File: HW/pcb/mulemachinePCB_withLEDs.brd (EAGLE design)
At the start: 68.6 x 54.6 mm, 33 parts, among them IC1 LD117AV50, IC2 MEGA8-P, J1 DCJ0202, Q1 16Mhz

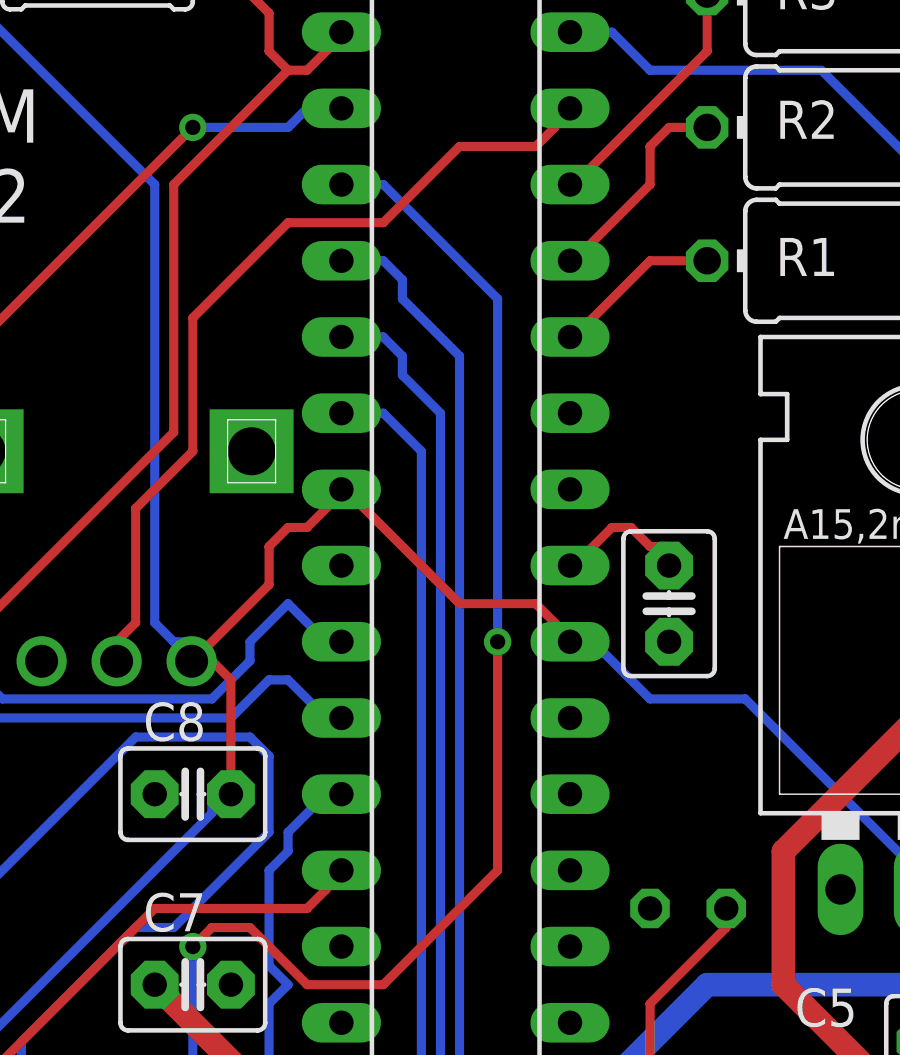
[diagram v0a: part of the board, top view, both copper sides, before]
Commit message: repinned LED and pump pins on MCU to use PWM digital pins. need to check and then reroute PCB and redo GND planes
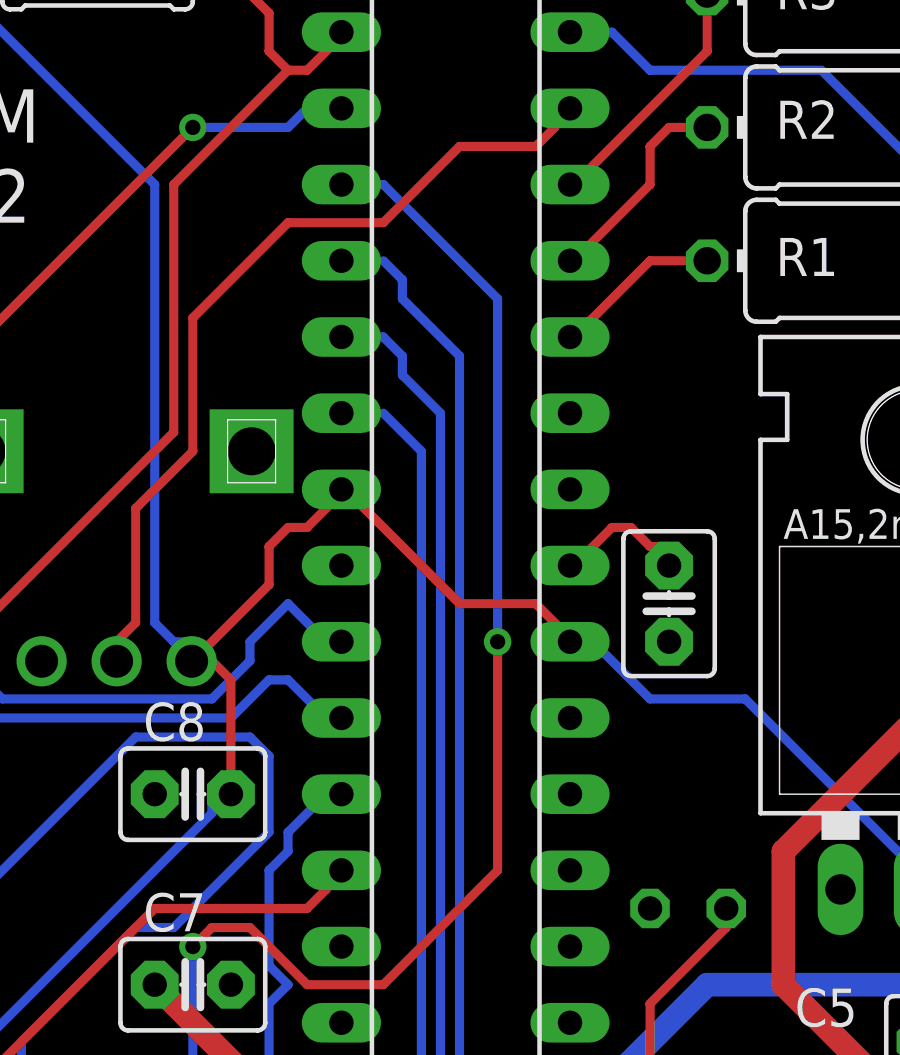
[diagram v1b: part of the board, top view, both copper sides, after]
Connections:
- net LED_YELLOW renamed LED_YELLOW_PWM
- removed net LED_GREEN: IC2.4, R6.1
- removed net PUMP_GB: IC2.25, R2.1
- removed net PUMP_LIME: IC2.26, R3.1
- removed net PUMP_VODKA: IC2.24, R1.1
- new net LED_GREEN_PWM: IC2.11, R6.1
- new net LED_ORANGE_PWM: IC2.12
- new net PUMP_GB_PWM: IC2.16, R2.1
- new net PUMP_LIME_PWM: IC2.17, R3.1
- new net PUMP_VODKA_PWM: IC2.15, R1.1
- net CUPSENSOR: now also IC2.6; no longer IC2.11
- net LED_ORANGE: no longer IC2.6
- net MANUALOVERRIDE: now also IC2.13; no longer IC2.12
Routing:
- net LED_GREEN: track 52.4 -> 0.00 mm, vias 1 -> 0
- net LED_GREEN_PWM: track 0.00 -> 51.0 mm, vias 0 -> 1
- net PUMP_LIME: track 8.32 -> 0.00 mm
- net PUMP_LIME_PWM: track 0.00 -> 8.19 mm
- net PUMP_GB: track 7.16 -> 0.00 mm
- net PUMP_GB_PWM: track 0.00 -> 7.03 mm
- net PUMP_VODKA: track 5.62 -> 0.00 mm
- net PUMP_VODKA_PWM: track 0.00 -> 5.50 mm
- net LED_ORANGE: track 27.7 -> 26.3 mm
- net CUPSENSOR: track 50.6 -> 50.1 mm
- net MANUALOVERRIDE: track 30.7 -> 30.1 mm
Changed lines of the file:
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@@
 <contactref element="T1" pad="E"/>
 <contactref element="T2" pad="E"/>
-<contactref element="T3" pad="E"/>
 <contactref element="C5" pad="2"/>
 <contactref element="C6" pad="-"/>
@@
 <contactref element="C3" pad="2"/>
 <contactref element="C2" pad="2"/>
-<wire x1="5.3594" y1="10.8712" x2="5.3594" y2="4.3688" width="0" layer="19" extent="1-1"/>
+<contactref element="T3" pad="E"/>
+<wire x1="55.88" y1="51.435" x2="60.96" y2="51.435" width="0" layer="19" extent="1-1"/>
+<wire x1="50.8" y1="51.435" x2="55.88" y2="51.435" width="0" layer="19" extent="1-1"/>
+<wire x1="62.865" y1="41.91" x2="60.96" y2="51.435" width="0" layer="19" extent="1-1"/>
+<wire x1="62.865" y1="33.02" x2="62.865" y2="41.91" width="0" layer="19" extent="1-1"/>
+<wire x1="58.42" y1="21.59" x2="62.865" y2="33.02" width="0" layer="19" extent="1-1"/>
+<wire x1="50.84" y1="29.83" x2="58.42" y2="21.59" width="0" layer="19" extent="1-1"/>
+<wire x1="56.4388" y1="10.414" x2="58.42" y2="21.59" width="0" layer="19" extent="1-1"/>
+<wire x1="44.577" y1="17.145" x2="56.4388" y2="10.414" width="0" layer="19" extent="1-1"/>
+<wire x1="39.37" y1="22.225" x2="44.577" y2="17.145" width="0" layer="19" extent="1-1"/>
+<wire x1="33.02" y1="21.59" x2="39.37" y2="22.225" width="0" layer="19" extent="1-1"/>
+<wire x1="33.655" y1="30.48" x2="33.02" y2="21.59" width="0" layer="19" extent="1-1"/>
+<wire x1="30.353" y1="35.56" x2="33.655" y2="30.48" width="0" layer="19" extent="1-1"/>
+<wire x1="22.733" y1="33.02" x2="30.353" y2="35.56" width="0" layer="19" extent="1-1"/>
+<wire x1="16.51" y1="25.4" x2="22.733" y2="33.02" width="0" layer="19" extent="1-1"/>
+<wire x1="12.74" y1="29.83" x2="16.51" y2="25.4" width="0" layer="19" extent="1-1"/>
+<wire x1="19.05" y1="19.05" x2="16.51" y2="25.4" width="0" layer="19" extent="1-1"/>
+<wire x1="4.953" y1="27.94" x2="12.74" y2="29.83" width="0" layer="19" extent="1-1"/>
+<wire x1="7.62" y1="21.59" x2="4.953" y2="27.94" width="0" layer="19" extent="1-1"/>
+<wire x1="5.3594" y1="10.8712" x2="7.62" y2="21.59" width="0" layer="19" extent="1-1"/>
+<wire x1="5.3594" y1="4.3688" x2="5.3594" y2="10.8712" width="0" layer="19" extent="1-1"/>
+<wire x1="2.54" y1="3.048" x2="5.3594" y2="4.3688" width="0" layer="19" extent="1-1"/>
+<wire x1="35.026" y1="10.668" x2="33.02" y2="21.59" width="0" layer="19" extent="1-1"/>
+<wire x1="30.226" y1="7.668" x2="35.026" y2="10.668" width="0" layer="19" extent="1-1"/>
+<wire x1="4.953" y1="44.45" x2="4.953" y2="27.94" width="0" layer="19" extent="1-1"/>
 </signal>
 <signal name="VCC" class="1">
@@
 <signal name="CUPSENSOR">
 <contactref element="X2" pad="7"/>
-<contactref element="IC2" pad="11"/>
 <wire x1="20.955" y1="24.13" x2="22.225" y2="25.4" width="0.3048" layer="16"/>
 <wire x1="20.955" y1="23.495" x2="20.955" y2="24.13" width="0.3048" layer="16"/>
@@
 <wire x1="51.435" y1="7.62" x2="34.29" y2="7.62" width="0.3048" layer="16"/>
 <wire x1="53.975" y1="10.16" x2="51.435" y2="7.62" width="0.3048" layer="16"/>
-<wire x1="22.225" y1="25.4" x2="22.733" y2="25.4" width="0.3048" layer="16"/>
 <wire x1="53.975" y1="10.16" x2="53.6956" y2="10.414" width="0.3048" layer="16"/>
+<contactref element="IC2" pad="6"/>
+<wire x1="22.225" y1="25.4" x2="22.733" y2="38.1" width="0" layer="19" extent="16-16"/>
 </signal>
 <signal name="N$12">
@@
 </signal>
 <signal name="MANUALOVERRIDE">
-<contactref element="IC2" pad="12"/>
 <contactref element="S2" pad="3"/>
 <contactref element="S2" pad="4"/>
@@
 <wire x1="8.89" y1="12.7" x2="8.89" y2="13.97" width="0.3048" layer="1"/>
 <wire x1="10.16" y1="11.43" x2="8.89" y2="12.7" width="0.3048" layer="1"/>
-<wire x1="22.225" y1="22.86" x2="22.733" y2="22.86" width="0.3048" layer="1"/>
 <wire x1="10.16" y1="11.43" x2="9.8806" y2="10.8712" width="0.3048" layer="1"/>
 <wire x1="9.525" y1="5.715" x2="9.525" y2="4.445" width="0.3048" layer="1"/>
@@
 <wire x1="9.525" y1="4.445" x2="9.8806" y2="4.3688" width="0.3048" layer="1"/>
 <wire x1="9.525" y1="11.43" x2="9.8806" y2="10.8712" width="0.3048" layer="1"/>
-</signal>
-<signal name="PUMP_VODKA">
-<contactref element="IC2" pad="24"/>
+<contactref element="IC2" pad="13"/>
+<wire x1="22.225" y1="22.86" x2="22.733" y2="20.32" width="0" layer="19" extent="1-1"/>
+</signal>
+<signal name="PUMP_VODKA_PWM">
 <contactref element="R1" pad="1"/>
 <wire x1="33.02" y1="43.18" x2="30.48" y2="40.64" width="0.3048" layer="1"/>
 <wire x1="34.925" y1="43.18" x2="33.02" y2="43.18" width="0.3048" layer="1"/>
-<wire x1="30.48" y1="40.64" x2="30.353" y2="40.64" width="0.3048" layer="1"/>
-</signal>
-<signal name="PUMP_GB">
-<contactref element="IC2" pad="25"/>
+<contactref element="IC2" pad="15"/>
+<wire x1="30.353" y1="17.78" x2="30.48" y2="40.64" width="0" layer="19" extent="1-1"/>
+</signal>
+<signal name="PUMP_GB_PWM">
 <contactref element="R2" pad="1"/>
 <wire x1="33.02" y1="45.72" x2="30.48" y2="43.18" width="0.3048" layer="1"/>
@@
 <wire x1="33.655" y1="47.625" x2="33.02" y2="46.99" width="0.3048" layer="1"/>
 <wire x1="34.925" y1="47.625" x2="33.655" y2="47.625" width="0.3048" layer="1"/>
-<wire x1="30.48" y1="43.18" x2="30.353" y2="43.18" width="0.3048" layer="1"/>
-</signal>
-<signal name="PUMP_LIME">
-<contactref element="IC2" pad="26"/>
+<contactref element="IC2" pad="16"/>
+<wire x1="30.353" y1="20.32" x2="30.48" y2="43.18" width="0" layer="19" extent="1-1"/>
+</signal>
+<signal name="PUMP_LIME_PWM">
 <contactref element="R3" pad="1"/>
 <wire x1="34.925" y1="50.165" x2="30.48" y2="45.72" width="0.3048" layer="1"/>
 <wire x1="34.925" y1="52.07" x2="34.925" y2="50.165" width="0.3048" layer="1"/>
-<wire x1="30.48" y1="45.72" x2="30.353" y2="45.72" width="0.3048" layer="1"/>
+<contactref element="IC2" pad="17"/>
+<wire x1="30.353" y1="22.86" x2="30.48" y2="45.72" width="0" layer="19" extent="1-1"/>
 </signal>
 <signal name="PUMP_LIME_VCC" class="1">
@@
 <wire x1="57.15" y1="15.24" x2="55.245" y2="17.145" width="0.7874" layer="1"/>
 </signal>
-<signal name="LED_GREEN">
+<signal name="LED_GREEN_PWM">
 <contactref element="R6" pad="1"/>
-<contactref element="IC2" pad="4"/>
-<wire x1="24.13" y1="43.18" x2="22.733" y2="43.18" width="0.3048" layer="16"/>
 <wire x1="24.765" y1="42.545" x2="24.13" y2="43.18" width="0.3048" layer="16"/>
 <wire x1="24.765" y1="41.91" x2="24.765" y2="42.545" width="0.3048" layer="16"/>
@@
 <wire x1="12.065" y1="3.175" x2="17.78" y2="3.175" width="0.3048" layer="1"/>
 <via x="27.305" y="14.605" extent="1-16" drill="0.508"/>
-</signal>
-<signal name="LED_YELLOW">
+<contactref element="IC2" pad="11"/>
+<wire x1="27.305" y1="14.605" x2="22.733" y2="25.4" width="0" layer="19" extent="1-1"/>
+</signal>
+<signal name="LED_YELLOW_PWM">
 <contactref element="R5" pad="1"/>
 <contactref element="IC2" pad="5"/>
@@
 <signal name="LED_ORANGE">
 <contactref element="R4" pad="1"/>
-<contactref element="IC2" pad="6"/>
-<wire x1="24.13" y1="38.1" x2="22.733" y2="38.1" width="0.3048" layer="16"/>
 <wire x1="25.4" y1="36.83" x2="24.13" y2="38.1" width="0.3048" layer="16"/>
 <wire x1="25.4" y1="14.605" x2="25.4" y2="36.83" width="0.3048" layer="16"/>
@@
 <wire x1="24.765" y1="12.573" x2="24.765" y2="13.97" width="0.3048" layer="16"/>
 </signal>
+<signal name="LED_ORANGE_PWM">
+<contactref element="IC2" pad="12"/>
+</signal>
 </signals>

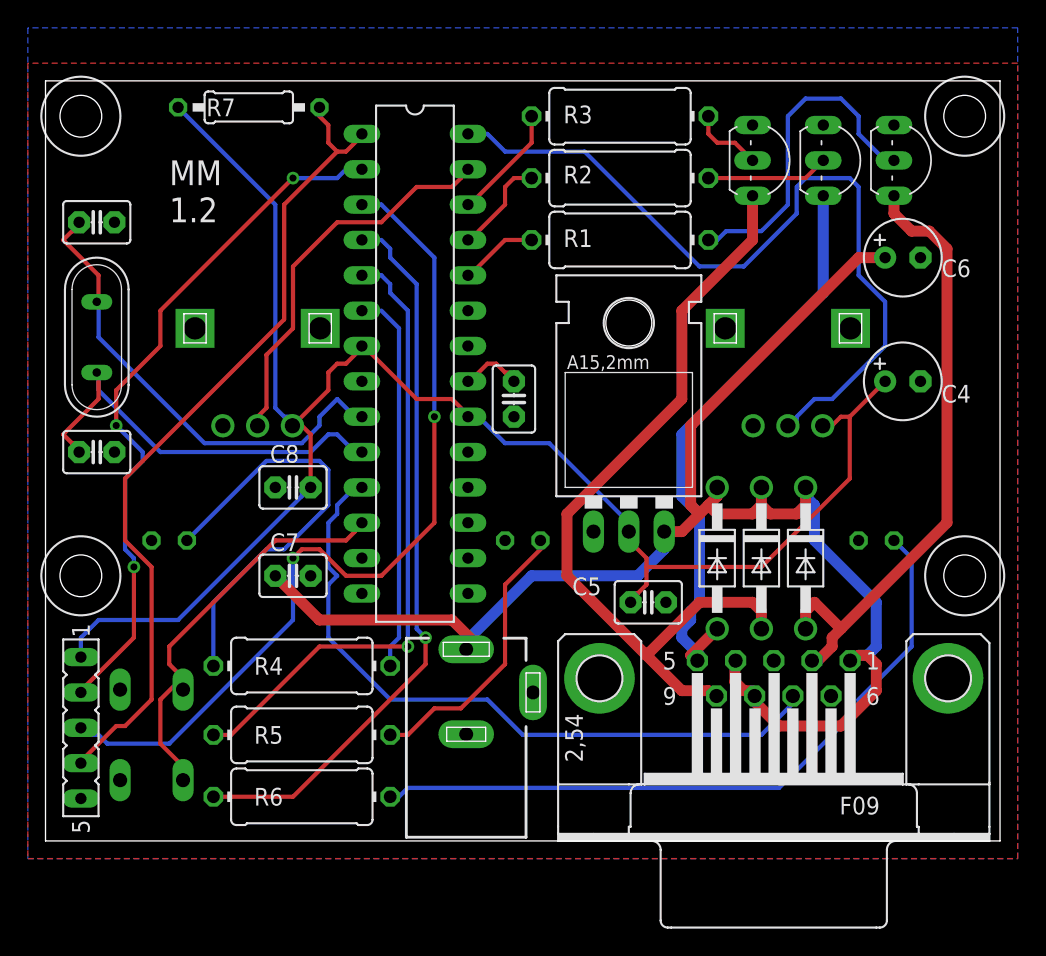
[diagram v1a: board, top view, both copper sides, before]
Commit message: finished positioning components, rerouted and made ground planes
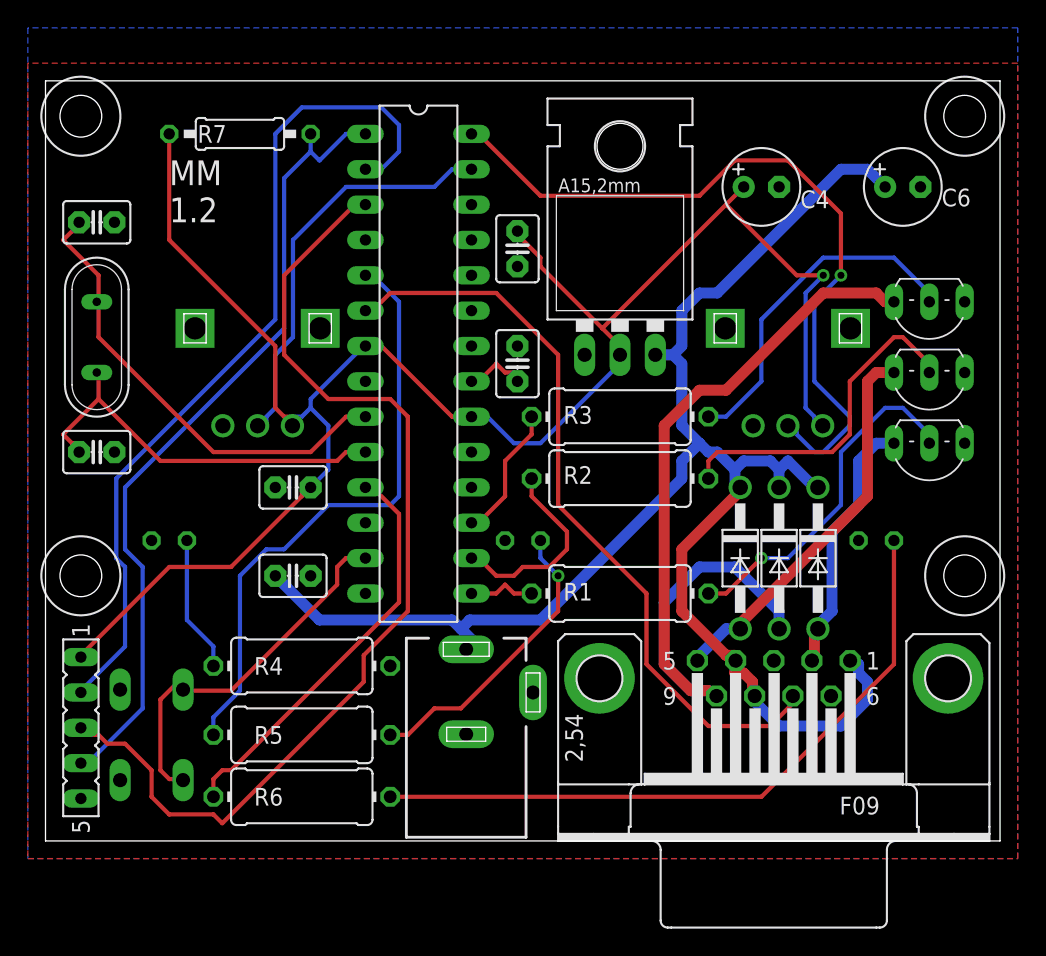
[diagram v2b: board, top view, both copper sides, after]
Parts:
- moved C5 27.1 mm to (33.9, 42.5), turned to 270 degrees
- moved R1 25.4 mm to (41.3, 17.8)
- moved T1 21.6 mm to (63.5, 27.3), turned to 180 degrees
- moved R2 21.6 mm to (41.3, 26.0)
- moved R3 21.6 mm to (41.3, 30.5)
- moved T2 17.7 mm to (63.5, 32.4), turned to 180 degrees
- moved C4 17.3 mm to (51.4, 47.0)
- moved T3 16.2 mm to (63.5, 37.5), turned to 180 degrees
- moved IC1 12.7 mm to (41.3, 38.7)
- moved C6 5.08 mm to (61.6, 47.0)
- moved C1 2.55 mm to (33.9, 34.3), turned to 90 degrees
- moved R7 2.01 mm to (14.0, 50.8)
- moved D2 1.65 mm to (49.9, 20.3)
- moved D3 1.27 mm to (52.7, 20.3)
- moved D1 0.89 mm to (55.5, 20.3)
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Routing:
- net LED_ORANGE: track 26.3 -> 0.00 mm
- net PUMP_VODKA_VCC: track 45.1 -> 19.3 mm
- net LED_GREEN_PWM: track 51.0 -> 29.4 mm, vias 1 -> 0
- net ORANGE: track 31.1 -> 9.81 mm
- net N$5: track 5.23 -> 24.9 mm
- net N$6: track 8.78 -> 24.5 mm
- net PUMP_GB_VCC: track 42.5 -> 28.4 mm
- net 5V: track 123.3 -> 135.5 mm, vias 0 -> 1
- net RX: track 50.6 -> 61.5 mm, vias 3 -> 0
- net TX: track 62.8 -> 73.5 mm, vias 2 -> 0
- net PUMP_GB_PWM: track 7.03 -> 14.3 mm
- net VCC: track 113.0 -> 120.1 mm
- net PUMP_LIME_VCC: track 58.5 -> 63.5 mm
- net CUPSENSOR: track 50.1 -> 54.9 mm
- net SOURRPOT: track 58.8 -> 54.5 mm, vias 0 -> 1
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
